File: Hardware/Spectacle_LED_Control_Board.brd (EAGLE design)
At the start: 25.4 x 55.9 mm, 44 parts, among them J3 USB-MICROB, J4 AUDIO-JACK3, J8 AUDIO-JACK3, U1 CY8C4146LQI-S422, U2 3.3V/150mA, U4 SN74LVC1G66, U5 SN74LVC1G66

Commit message: Changes from review
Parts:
- moved C10 10.6 mm to (18.5, 12.1), turned to 180 degrees
- moved C9 9.02 mm to (16.6, 7.49), turned to 180 degrees
- moved U4 0.38 mm to (16.1, 5.21)
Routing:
- net VIN: track 77.5 -> 54.4 mm, vias 2 -> 0
- net GND: vias 7 -> 8

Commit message: File changes from checklist first pass
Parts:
- moved FD1 4.58 mm to (1.27, 5.08)
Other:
- board text added: "v02"
- board text removed: "v01"
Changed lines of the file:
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@@
 <?xml version="1.0" encoding="utf-8"?>
 <!DOCTYPE eagle SYSTEM "eagle.dtd">
-<eagle version="7.6.0">
+<eagle version="7.7.0">
 <drawing>
 <settings>
@@
 <grid distance="0.05" unitdist="inch" unit="inch" style="lines" multiple="1" display="yes" altdistance="0.005" altunitdist="inch" altunit="inch"/>
 <layers>
-<layer number="1" name="Top" color="4" fill="1" visible="yes" active="yes"/>
+<layer number="1" name="Top" color="4" fill="1" visible="no" active="yes"/>
 <layer number="2" name="Route2" color="1" fill="3" visible="no" active="yes"/>
 <layer number="15" name="Route15" color="4" fill="6" visible="no" active="yes"/>
-<layer number="16" name="Bottom" color="1" fill="1" visible="no" active="yes"/>
+<layer number="16" name="Bottom" color="1" fill="1" visible="yes" active="yes"/>
 <layer number="17" name="Pads" color="2" fill="1" visible="yes" active="yes"/>
 <layer number="18" name="Vias" color="2" fill="1" visible="yes" active="yes"/>
 <layer number="19" name="Unrouted" color="6" fill="1" visible="yes" active="yes"/>
 <layer number="20" name="Dimension" color="15" fill="1" visible="yes" active="yes"/>
-<layer number="21" name="tPlace" color="15" fill="1" visible="yes" active="yes"/>
-<layer number="22" name="bPlace" color="14" fill="1" visible="no" active="yes"/>
-<layer number="23" name="tOrigins" color="15" fill="1" visible="yes" active="yes"/>
-<layer number="24" name="bOrigins" color="15" fill="1" visible="no" active="yes"/>
+<layer number="21" name="tPlace" color="16" fill="1" visible="no" active="yes"/>
+<layer number="22" name="bPlace" color="14" fill="1" visible="yes" active="yes"/>
+<layer number="23" name="tOrigins" color="15" fill="1" visible="no" active="yes"/>
+<layer number="24" name="bOrigins" color="15" fill="1" visible="yes" active="yes"/>
 <layer number="25" name="tNames" color="7" fill="1" visible="no" active="yes"/>
 <layer number="26" name="bNames" color="7" fill="1" visible="no" active="yes"/>
@@
 <text x="18.669" y="49.149" size="1.778" layer="21" font="vector" ratio="15" align="center">2</text>
 <text x="90.17" y="45.72" size="1.778" layer="51" font="vector" ratio="15">Dia Campbell and Mike Hord</text>
-<text x="20.32" y="0.762" size="1.27" layer="16" font="vector" ratio="15" rot="MR0">v01</text>
+<text x="20.32" y="0.762" size="1.27" layer="16" font="vector" ratio="15" rot="MR0">v02</text>
 <text x="0.635" y="50.038" size="1.27" layer="1" font="vector" ratio="15">1</text>
 <text x="1.778" y="50.038" size="1.27" layer="2" font="vector" ratio="15">2</text>
@@
 <attribute name="PROD_ID" value="CONN-11752" x="12.7" y="53.848" size="1.778" layer="27" font="vector" ratio="15" rot="R270" display="off"/>
 </element>
-<element name="J5" library="SparkFun-Connectors" package="JST-3-PTH-VERT" value="" x="18.415" y="43.688" rot="R270"/>
-<element name="J6" library="SparkFun-Connectors" package="JST-3-PTH-VERT" value="" x="7.112" y="43.688" rot="R270"/>
-<element name="J7" library="SparkFun-Connectors" package="JST-3-PTH-VERT" value="" x="12.827" y="43.688" rot="R270"/>
+<element name="J5" library="SparkFun-Connectors" package="JST-3-PTH-VERT" value="" x="18.415" y="43.688" rot="R270">
+<attribute name="PROD_ID" value="CONN-13230" x="18.415" y="43.688" size="1.778" layer="27" rot="R270" display="off"/>
+</element>
+<element name="J6" library="SparkFun-Connectors" package="JST-3-PTH-VERT" value="" x="7.112" y="43.688" rot="R270">
+<attribute name="PROD_ID" value="CONN-13230" x="7.112" y="43.688" size="1.778" layer="27" rot="R270" display="off"/>
+</element>
+<element name="J7" library="SparkFun-Connectors" package="JST-3-PTH-VERT" value="" x="12.827" y="43.688" rot="R270">
+<attribute name="PROD_ID" value="CONN-13230" x="12.827" y="43.688" size="1.778" layer="27" rot="R270" display="off"/>
+</element>
 <element name="U$1" library="SparkFun-Aesthetics" package="FOUR_LAYER_WARNING" value="FOUR_LAYER_WARNING" x="39.37" y="54.61"/>
 <element name="LOGO1" library="SparkFun-Aesthetics" package="OSHW-LOGO-S" value="OSHW-LOGOS" x="23.241" y="48.387"/>
 <element name="LOGO2" library="SparkFun-Aesthetics" package="SFE_LOGO_NAME_FLAME_.1" value="SFE_LOGO_NAME_FLAME.1_INCH" x="4.064" y="0.254"/>
 <element name="J8" library="SparkFun-Connectors" package="AUDIO-JACK-TRRS-SMD" value="AUDIO-JACK3" x="0" y="10.16"/>
-<element name="FD1" library="SparkFun-Aesthetics" package="MICRO-FIDUCIAL" value="FIDUCIALUFIDUCIAL" x="5.08" y="7.62"/>
+<element name="FD1" library="SparkFun-Aesthetics" package="MICRO-FIDUCIAL" value="FIDUCIALUFIDUCIAL" x="1.27" y="5.08"/>
 <element name="FD2" library="SparkFun-Aesthetics" package="MICRO-FIDUCIAL" value="FIDUCIALUFIDUCIAL" x="20.32" y="50.8"/>
 <element name="D5" library="SparkFun-DiscreteSemi" package="SOD-323" value="BAT20J" x="21.59" y="21.209" rot="R270">
 <attribute name="PROD_ID" value="DIO-11623" x="26.67" y="25.019" size="1.778" layer="27" font="vector" ratio="15" rot="R270" display="off"/>
 </element>
-<element name="J9" library="SparkFun-Connectors" package="1X06_NO_SILK" value="" x="1.27" y="30.861" rot="R90">
-<attribute name="PROD_ID" value="CONN-08437" x="1.27" y="30.861" size="1.778" layer="27" font="vector" ratio="15" rot="R90" display="off"/>
-</element>
+<element name="J9" library="SparkFun-Connectors" package="1X06_NO_SILK" value="" x="1.27" y="30.861" rot="R90"/>
 <element name="C9" library="SparkFun-Capacitors" package="0402-CAP" value="0.1uF" x="16.637" y="7.493" rot="R180">
 <attribute name="PROD_ID" value="CAP-12416" x="16.637" y="7.493" size="1.778" layer="27" font="vector" ratio="15" rot="R180" display="off"/>

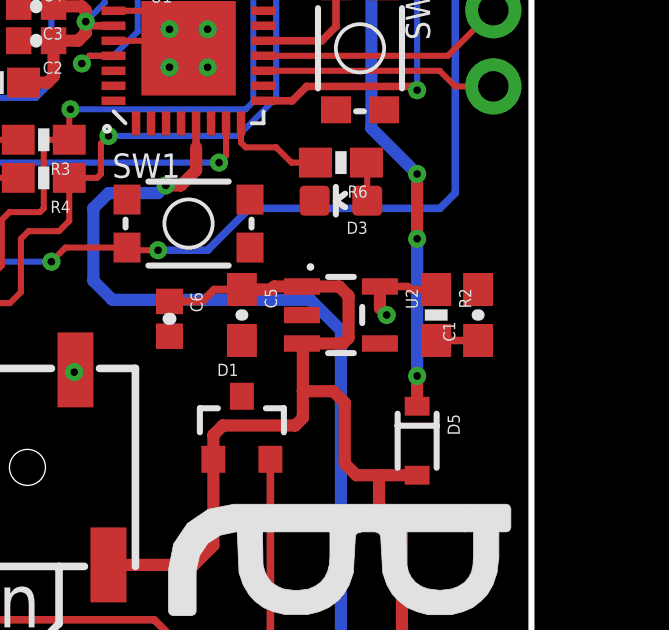
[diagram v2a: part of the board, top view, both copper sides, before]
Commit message: Chg VREG to APK2112
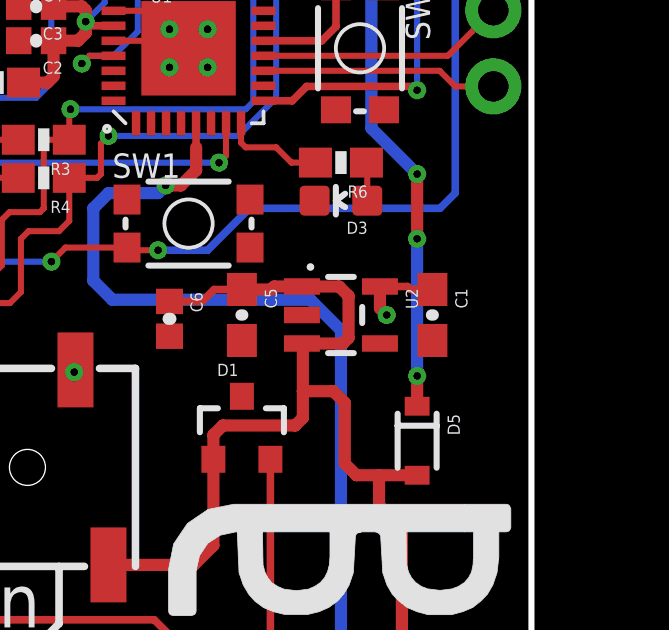
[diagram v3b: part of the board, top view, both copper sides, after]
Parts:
- removed R2: 0.27, SparkFun-Resistors:0603-RES
- U2: value 3.3V/150mA -> 3.3V
- moved C1 1.52 mm to (22.1, 25.4), turned to 270 degrees
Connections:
- removed net N$3: C1.1, R2.2
- net 3.3V: now also C1.1; no longer R2.1
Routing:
- net N$3: track 1.40 -> 0.00 mm
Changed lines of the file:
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@@
 <grid distance="0.05" unitdist="inch" unit="inch" style="lines" multiple="1" display="yes" altdistance="0.005" altunitdist="inch" altunit="inch"/>
 <layers>
-<layer number="1" name="Top" color="4" fill="1" visible="no" active="yes"/>
+<layer number="1" name="Top" color="4" fill="1" visible="yes" active="yes"/>
 <layer number="2" name="Route2" color="1" fill="3" visible="no" active="yes"/>
 <layer number="15" name="Route15" color="4" fill="6" visible="no" active="yes"/>
@@
 <layer number="19" name="Unrouted" color="6" fill="1" visible="yes" active="yes"/>
 <layer number="20" name="Dimension" color="15" fill="1" visible="yes" active="yes"/>
-<layer number="21" name="tPlace" color="16" fill="1" visible="no" active="yes"/>
+<layer number="21" name="tPlace" color="16" fill="1" visible="yes" active="yes"/>
 <layer number="22" name="bPlace" color="14" fill="1" visible="yes" active="yes"/>
-<layer number="23" name="tOrigins" color="15" fill="1" visible="no" active="yes"/>
+<layer number="23" name="tOrigins" color="15" fill="1" visible="yes" active="yes"/>
 <layer number="24" name="bOrigins" color="15" fill="1" visible="yes" active="yes"/>
 <layer number="25" name="tNames" color="7" fill="1" visible="no" active="yes"/>
@@
 <layer number="43" name="vRestrict" color="2" fill="10" visible="no" active="yes"/>
 <layer number="44" name="Drills" color="7" fill="1" visible="no" active="yes"/>
-<layer number="45" name="Holes" color="7" fill="1" visible="no" active="yes"/>
+<layer number="45" name="Holes" color="7" fill="1" visible="yes" active="yes"/>
 <layer number="46" name="Milling" color="3" fill="1" visible="no" active="yes"/>
 <layer number="47" name="Measures" color="7" fill="1" visible="no" active="yes"/>
 <layer number="48" name="Document" color="7" fill="1" visible="no" active="yes"/>
 <layer number="49" name="Reference" color="7" fill="1" visible="no" active="yes"/>
-<layer number="51" name="tDocu" color="6" fill="1" visible="no" active="yes"/>
+<layer number="51" name="tDocu" color="6" fill="1" visible="yes" active="yes"/>
 <layer number="52" name="bDocu" color="7" fill="1" visible="no" active="yes"/>
 <layer number="3" name="Route3" color="4" fill="3" visible="no" active="no"/>
@@
 <attribute name="PROD_ID" value="IC-13286" x="13.97" y="34.29" size="1.778" layer="27" display="off"/>
 </element>
-<element name="U2" library="SparkFun-PowerIC" package="SOT23-5" value="3.3V/150mA" x="19.05" y="25.4" rot="R270">
-<attribute name="PROD_ID" value="VREG-00822" x="19.05" y="25.4" size="1.778" layer="27" font="vector" ratio="15" rot="R270" display="off"/>
+<element name="U2" library="SparkFun-PowerIC" package="SOT23-5" value="3.3V" x="19.05" y="25.4" rot="R270">
+<attribute name="PROD_ID" value="VREG-12457" x="19.05" y="25.4" size="1.778" layer="27" font="vector" ratio="15" rot="R270" display="off"/>
 </element>
 <element name="R1" library="SparkFun-Resistors" package="0603-RES" value="10K" x="8.128" y="38.735" rot="R180">
 <attribute name="PROD_ID" value="RES-00824" x="8.128" y="38.735" size="1.778" layer="27" font="vector" ratio="15" rot="R180" display="off"/>
 </element>
-<element name="R2" library="SparkFun-Resistors" package="0603-RES" value="0.27" x="22.225" y="25.4" rot="R270">
-<attribute name="PROD_ID" value="RES-08787" x="22.225" y="25.4" size="1.778" layer="27" font="vector" ratio="15" rot="R270" display="off"/>
-</element>
-<element name="C1" library="SparkFun-Capacitors" package="0603-CAP" value="2.2uF" x="23.622" y="25.4" rot="R90">
-<attribute name="PROD_ID" value="CAP-07888" x="23.622" y="25.4" size="1.778" layer="27" font="vector" ratio="15" rot="R90" display="off"/>
+<element name="C1" library="SparkFun-Capacitors" package="0603-CAP" value="2.2uF" x="22.098" y="25.4" rot="R270">
+<attribute name="PROD_ID" value="CAP-07888" x="22.098" y="25.4" size="1.778" layer="27" font="vector" ratio="15" rot="R270" display="off"/>
 </element>
 <element name="C2" library="SparkFun-Capacitors" package="0402-CAP" value="1.0uF" x="8.89" y="34.544" rot="R180">
@@
 <wire x1="22.86" y1="37.592" x2="23.368" y2="38.1" width="0.254" layer="16"/>
 <wire x1="24.13" y1="38.1" x2="23.368" y2="38.1" width="0.254" layer="16"/>
-</signal>
-<signal name="N$3">
-<contactref element="R2" pad="2"/>
-<contactref element="C1" pad="1"/>
-<wire x1="22.225" y1="24.55" x2="23.622" y2="24.55" width="0.254" layer="1"/>
 </signal>
 <signal name="VIN">
@@
 <contactref element="J2" pad="1"/>
 <contactref element="U2" pad="5"/>
-<contactref element="R2" pad="1"/>
 <contactref element="JP1" pad="2"/>
 <contactref element="U1" pad="27"/>
 <contactref element="R1" pad="2"/>
-<wire x1="20.3501" y1="26.35" x2="21.275" y2="26.35" width="0.254" layer="1"/>
-<wire x1="21.275" y1="26.35" x2="21.375" y2="26.25" width="0.254" layer="1"/>
-<wire x1="21.375" y1="26.25" x2="22.225" y2="26.25" width="0.254" layer="1"/>
 <wire x1="11.47" y1="35.04" x2="10.553" y2="35.04" width="0.254" layer="1"/>
 <wire x1="10.287" y1="34.544" x2="9.47" y2="34.544" width="0.4064" layer="1"/>
@@
 <wire x1="11.176" y1="37.719" x2="11.176" y2="35.814" width="0.2032" layer="16"/>
 <wire x1="11.176" y1="35.814" x2="10.541" y2="35.179" width="0.2032" layer="16"/>
+<contactref element="C1" pad="1"/>
+<wire x1="20.3501" y1="26.35" x2="21.275" y2="26.35" width="0.254" layer="1"/>
+<wire x1="21.275" y1="26.35" x2="21.375" y2="26.25" width="0.254" layer="1"/>
+<wire x1="22.098" y1="26.25" x2="21.375" y2="26.25" width="0.254" layer="1"/>
 </signal>
 <signal name="ISO_POUR">

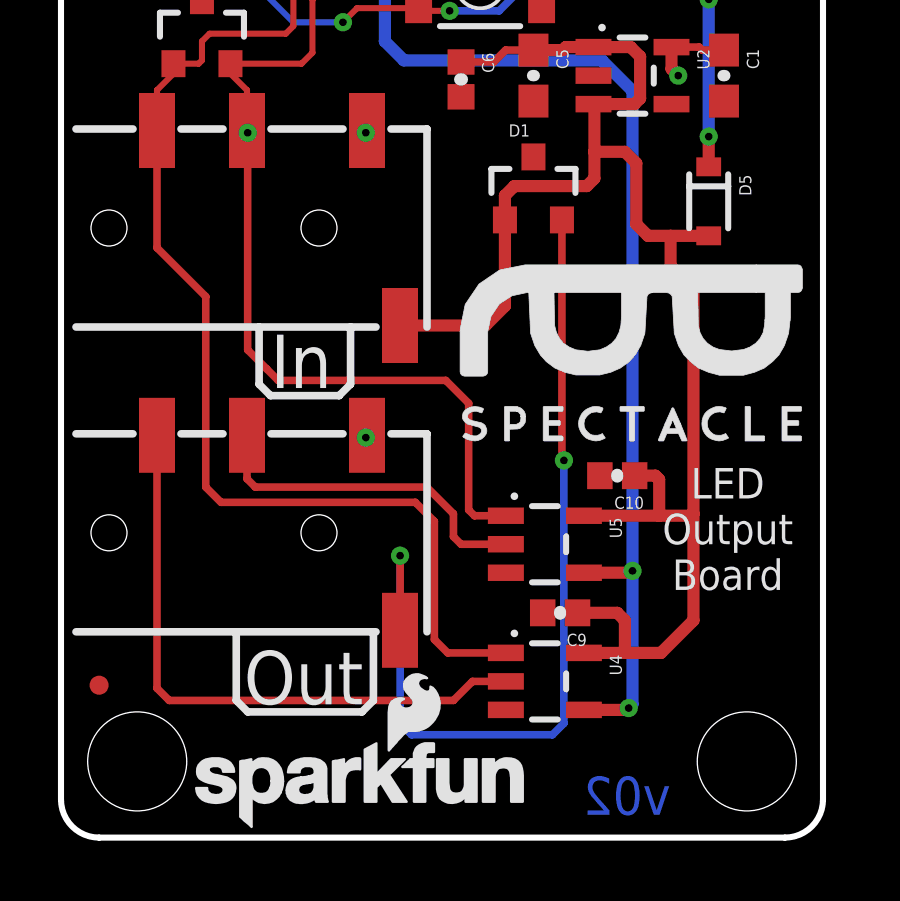
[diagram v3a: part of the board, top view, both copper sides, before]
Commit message: Fix VIN path per review
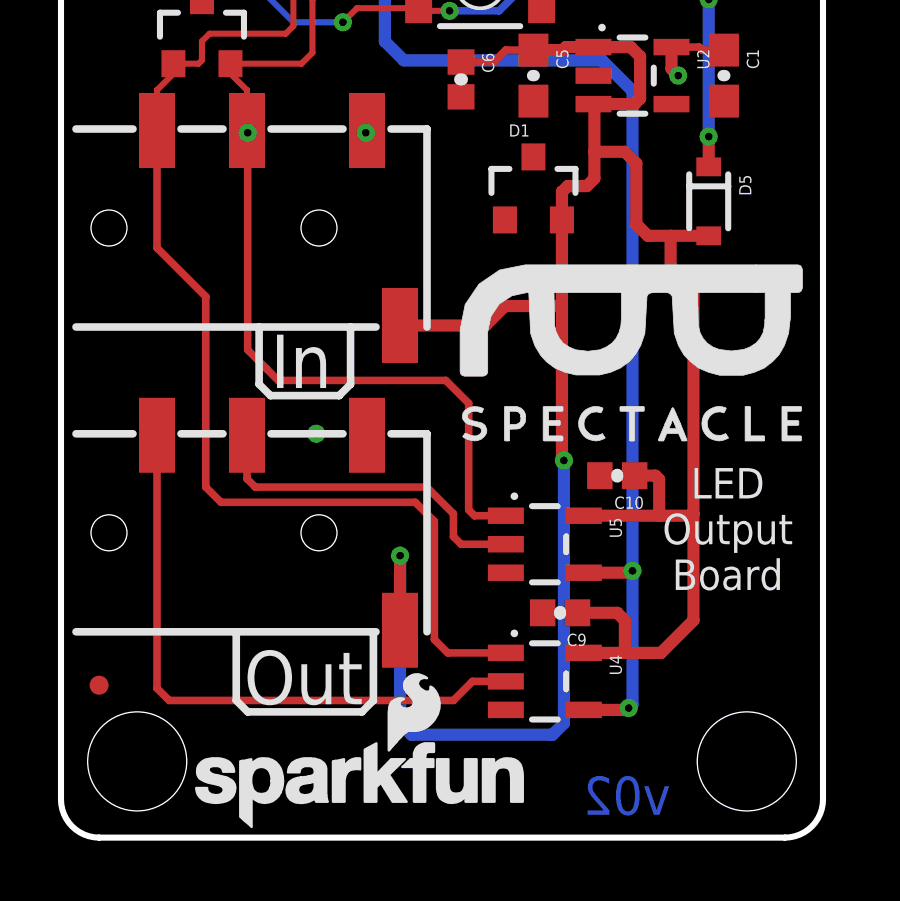
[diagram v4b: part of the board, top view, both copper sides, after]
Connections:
- removed net N$1: D1.2, J8.EARTH
- net VIN: now also D1.2, J8.EARTH; no longer D1.1
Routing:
- net N$1: track 30.7 -> 0.00 mm, vias 2 -> 0
- net VIN: track 54.4 -> 82.3 mm, vias 0 -> 2
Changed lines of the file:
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@@
 <wire x1="10.033" y1="4.191" x2="10.414" y2="4.572" width="0.254" layer="21"/>
 <wire x1="10.414" y1="4.572" x2="10.414" y2="6.731" width="0.254" layer="21"/>
+<rectangle x1="9.906" y1="14.605" x2="10.414" y2="14.859" layer="41"/>
+<rectangle x1="10.033" y1="12.065" x2="10.414" y2="12.192" layer="41"/>
 </plain>
 <attributes>
@@
 <contactref element="J5" pad="2"/>
 <contactref element="J6" pad="2"/>
-<via x="10.16" y="13.335" extent="1-16" drill="0.254"/>
+<via x="8.509" y="13.462" extent="1-16" drill="0.254"/>
 <via x="10.16" y="23.495" extent="1-16" drill="0.254"/>
 <contactref element="J9" pad="1"/>
@@
 <wire x1="14.82" y1="26.25" x2="14.423" y2="25.853" width="0.254" layer="1"/>
 <contactref element="D5" pad="A"/>
-<contactref element="D1" pad="1"/>
-<wire x1="14.798" y1="20.59" x2="14.798" y2="21.402" width="0.4064" layer="1"/>
-<wire x1="14.798" y1="21.402" x2="15.113" y2="21.717" width="0.4064" layer="1"/>
-<wire x1="15.113" y1="21.717" x2="17.526" y2="21.717" width="0.4064" layer="1"/>
 <contactref element="C9" pad="1"/>
 <contactref element="C10" pad="1"/>
@@
 <wire x1="11.3" y1="17.07" x2="14.149" y2="17.07" width="0.4064" layer="1"/>
 <wire x1="14.149" y1="17.07" x2="14.798" y2="17.719" width="0.4064" layer="1"/>
-<wire x1="14.798" y1="20.59" x2="14.798" y2="17.719" width="0.4064" layer="1"/>
+<contactref element="D1" pad="2"/>
+<contactref element="J8" pad="EARTH"/>
+<wire x1="16.698" y1="20.59" x2="16.698" y2="17.78" width="0.4064" layer="1"/>
+<wire x1="16.698" y1="17.78" x2="16.698" y2="12.639" width="0.4064" layer="1"/>
+<wire x1="16.698" y1="12.639" x2="16.764" y2="12.573" width="0.254" layer="1"/>
+<via x="16.764" y="12.573" extent="1-16" drill="0.254"/>
+<wire x1="16.764" y1="12.573" x2="16.764" y2="3.81" width="0.4064" layer="16"/>
+<wire x1="16.383" y1="3.429" x2="11.684" y2="3.429" width="0.4064" layer="16"/>
+<wire x1="11.684" y1="3.429" x2="11.303" y2="3.81" width="0.4064" layer="16"/>
+<wire x1="11.303" y1="3.81" x2="11.303" y2="9.398" width="0.4064" layer="16"/>
+<via x="11.303" y="9.398" extent="1-16" drill="0.254"/>
+<wire x1="11.303" y1="9.398" x2="11.303" y2="6.913" width="0.4064" layer="1"/>
+<wire x1="11.303" y1="6.913" x2="11.3" y2="6.91" width="0.254" layer="1"/>
+<wire x1="16.383" y1="3.429" x2="16.764" y2="3.81" width="0.4064" layer="16"/>
+<wire x1="14.798" y1="17.719" x2="16.637" y2="17.719" width="0.4064" layer="1"/>
+<wire x1="16.637" y1="17.719" x2="16.698" y2="17.78" width="0.4064" layer="1"/>
+<wire x1="16.698" y1="20.59" x2="16.698" y2="21.529" width="0.4064" layer="1"/>
+<wire x1="16.698" y1="21.529" x2="16.703" y2="21.529" width="0.4064" layer="1"/>
+<wire x1="16.703" y1="21.529" x2="16.891" y2="21.717" width="0.4064" layer="1"/>
+<wire x1="16.891" y1="21.717" x2="17.526" y2="21.717" width="0.4064" layer="1"/>
 </signal>
 <signal name="N$2">
@@
 <wire x1="10.672" y1="34.04" x2="10.414" y2="33.782" width="0.2032" layer="16"/>
 </signal>
-<signal name="N$1">
-<contactref element="D1" pad="2"/>
-<contactref element="J8" pad="EARTH"/>
-<wire x1="16.698" y1="20.59" x2="16.698" y2="12.639" width="0.254" layer="1"/>
-<wire x1="16.698" y1="12.639" x2="16.764" y2="12.573" width="0.254" layer="1"/>
-<via x="16.764" y="12.573" extent="1-16" drill="0.254"/>
-<wire x1="16.764" y1="12.573" x2="16.764" y2="3.81" width="0.254" layer="16"/>
-<wire x1="16.383" y1="3.429" x2="11.684" y2="3.429" width="0.254" layer="16"/>
-<wire x1="11.684" y1="3.429" x2="11.303" y2="3.81" width="0.254" layer="16"/>
-<wire x1="11.303" y1="3.81" x2="11.303" y2="9.398" width="0.254" layer="16"/>
-<via x="11.303" y="9.398" extent="1-16" drill="0.254"/>
-<wire x1="11.303" y1="9.398" x2="11.303" y2="6.913" width="0.254" layer="1"/>
-<wire x1="11.303" y1="6.913" x2="11.3" y2="6.91" width="0.254" layer="1"/>
-<wire x1="16.383" y1="3.429" x2="16.764" y2="3.81" width="0.254" layer="16"/>
-</signal>
 <signal name="I2C_OUT_EN">

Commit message: Change pullups to 4.7k
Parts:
- R3, R4: value 2.2k -> 4.7K
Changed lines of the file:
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@@
 <attribute name="PROD_ID" value="CAP-12416" x="13.335" y="25.273" size="1.778" layer="27" font="vector" ratio="15" rot="R270" display="off"/>
 </element>
-<element name="R3" library="SparkFun-Resistors" package="0603-RES" value="2.2k" x="9.144" y="31.242" rot="R180">
-<attribute name="PROD_ID" value="RES-08272" x="9.144" y="31.242" size="1.778" layer="27" font="vector" ratio="15" rot="R180" display="off"/>
+<element name="R3" library="SparkFun-Resistors" package="0603-RES" value="4.7K" x="9.144" y="31.242" rot="R180">
+<attribute name="PROD_ID" value="RES-07857" x="9.144" y="31.242" size="1.778" layer="27" font="vector" ratio="15" rot="R180" display="off"/>
 </element>
-<element name="R4" library="SparkFun-Resistors" package="0603-RES" value="2.2k" x="9.144" y="29.972" rot="R180">
-<attribute name="PROD_ID" value="RES-08272" x="9.144" y="29.972" size="1.778" layer="27" font="vector" ratio="15" rot="R180" display="off"/>
+<element name="R4" library="SparkFun-Resistors" package="0603-RES" value="4.7K" x="9.144" y="29.972" rot="R180">
+<attribute name="PROD_ID" value="RES-07857" x="9.144" y="29.972" size="1.778" layer="27" font="vector" ratio="15" rot="R180" display="off"/>
 </element>
 <element name="JP1" library="SparkFun-Passives" package="PAD-JUMPER-3-NC_BY_PASTE_YES_SILK_FULL_BOX" value="JUMPER-PAD-3-NC_BY_PASTE" x="6.477" y="30.607" rot="R90"/>
